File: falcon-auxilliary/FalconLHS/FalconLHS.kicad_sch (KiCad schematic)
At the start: 18 parts, among them J1 100mil, U1 AL8843QSP-13, U2 AL8843QSP-13

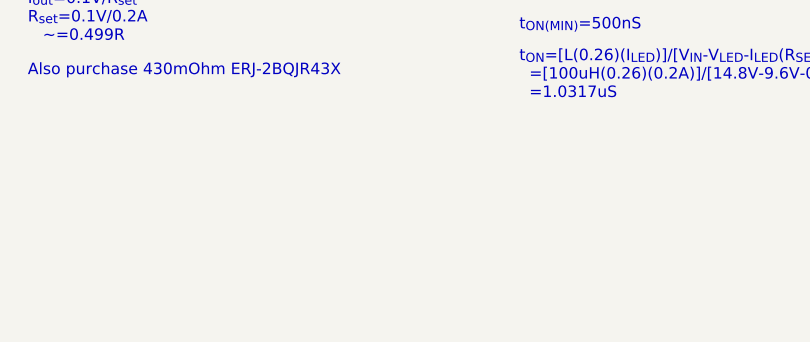
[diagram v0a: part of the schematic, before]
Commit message: Fix missing mounting holes
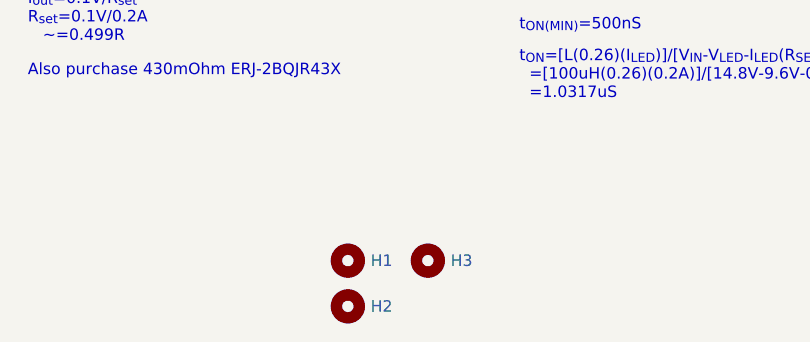
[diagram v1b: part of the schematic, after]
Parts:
- added H1, H2, H3: MountingHole, JetkovKiCADLib:MountingHole_2.7mm_M2.5_Clearanced, symbol Mechanical:MountingHole
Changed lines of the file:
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@@
   (symbol (lib_id "power:GND") (at 187.96 90.17 0) (unit 1)
     (in_bom yes) (on_board yes)
-    (property "Reference" "#PWR07" (id 0) (at 187.96 96.52 0)
+    (property "Reference" "#PWR08" (id 0) (at 187.96 96.52 0)
       (effects (font (size 1.27 1.27)) hide)
     )
@@
   (symbol (lib_id "power:GND") (at 148.59 66.04 0) (mirror y) (unit 1)
     (in_bom yes) (on_board yes)
-    (property "Reference" "#PWR04" (id 0) (at 148.59 72.39 0)
+    (property "Reference" "#PWR05" (id 0) (at 148.59 72.39 0)
       (effects (font (size 1.27 1.27)) hide)
     )
@@
   (symbol (lib_id "power:GND") (at 157.48 66.04 0) (unit 1)
     (in_bom yes) (on_board yes)
-    (property "Reference" "#PWR05" (id 0) (at 157.48 72.39 0)
+    (property "Reference" "#PWR06" (id 0) (at 157.48 72.39 0)
       (effects (font (size 1.27 1.27)) hide)
     )
@@
     (pin "1")
   )
+  (symbol (lib_id "Mechanical:MountingHole") (at 151.13 142.24 0) (unit 1)
+    (in_bom yes) (on_board yes) (fields_autoplaced)
+    (property "Reference" "H3" (id 0) (at 153.67 142.2399 0)
+      (effects (font (size 1.27 1.27)) (justify left))
+    )
+    (property "Value" "MountingHole" (id 1) (at 153.67 143.5099 0)
+      (effects (font (size 1.27 1.27)) (justify left) hide)
+    )
+    (property "Footprint" "JetkovKiCADLib:MountingHole_2.7mm_M2.5_Clearanced" (id 2) (at 151.13 142.24 0)
+      (effects (font (size 1.27 1.27)) hide)
+    )
+    (property "Datasheet" "~" (id 3) (at 151.13 142.24 0)
+      (effects (font (size 1.27 1.27)) hide)
+    )
+  )
   (symbol (lib_id "Device:D_Schottky_Small") (at 96.52 91.44 90) (mirror x) (unit 1)
     (in_bom yes) (on_board yes)
@@
     (pin "2")
   )
+  (symbol (lib_id "Mechanical:MountingHole") (at 142.24 147.32 0) (unit 1)
+    (in_bom yes) (on_board yes) (fields_autoplaced)
+    (property "Reference" "H2" (id 0) (at 144.78 147.3199 0)
+      (effects (font (size 1.27 1.27)) (justify left))
+    )
+    (property "Value" "MountingHole" (id 1) (at 144.78 148.5899 0)
+      (effects (font (size 1.27 1.27)) (justify left) hide)
+    )
+    (property "Footprint" "JetkovKiCADLib:MountingHole_2.7mm_M2.5_Clearanced" (id 2) (at 142.24 147.32 0)
+      (effects (font (size 1.27 1.27)) hide)
+    )
+    (property "Datasheet" "~" (id 3) (at 142.24 147.32 0)
+      (effects (font (size 1.27 1.27)) hide)
+    )
+  )
   (symbol (lib_id "JetkovKiCADLib:XQA LED 1616 SMD") (at 252.73 99.06 0) (mirror x) (unit 1)
     (in_bom yes) (on_board yes)
@@
   (symbol (lib_id "power:GND") (at 64.77 105.41 0) (unit 1)
     (in_bom yes) (on_board yes)
-    (property "Reference" "#PWR?" (id 0) (at 64.77 111.76 0)
+    (property "Reference" "#PWR03" (id 0) (at 64.77 111.76 0)
       (effects (font (size 1.27 1.27)) hide)
     )
@@
   (symbol (lib_id "JetkovKiCADLib:VSYS_SW") (at 187.96 74.93 0) (unit 1)
     (in_bom yes) (on_board yes) (fields_autoplaced)
-    (property "Reference" "#PWR06" (id 0) (at 187.96 78.74 0)
+    (property "Reference" "#PWR07" (id 0) (at 187.96 78.74 0)
       (effects (font (size 1.27 1.27)) hide)
     )
@@
   (symbol (lib_id "power:GND") (at 187.96 105.41 0) (unit 1)
     (in_bom yes) (on_board yes)
-    (property "Reference" "#PWR08" (id 0) (at 187.96 111.76 0)
+    (property "Reference" "#PWR09" (id 0) (at 187.96 111.76 0)
       (effects (font (size 1.27 1.27)) hide)
     )
@@
     (pin "3")
   )
+  (symbol (lib_id "Mechanical:MountingHole") (at 142.24 142.24 0) (unit 1)
+    (in_bom yes) (on_board yes) (fields_autoplaced)
+    (property "Reference" "H1" (id 0) (at 144.78 142.2399 0)
+      (effects (font (size 1.27 1.27)) (justify left))
+    )
+    (property "Value" "MountingHole" (id 1) (at 144.78 143.5099 0)
+      (effects (font (size 1.27 1.27)) (justify left) hide)
+    )
+    (property "Footprint" "JetkovKiCADLib:MountingHole_2.7mm_M2.5_Clearanced" (id 2) (at 142.24 142.24 0)
+      (effects (font (size 1.27 1.27)) hide)
+    )
+    (property "Datasheet" "~" (id 3) (at 142.24 142.24 0)
+      (effects (font (size 1.27 1.27)) hide)
+    )
+  )
   (symbol (lib_id "JetkovKiCADLib:XQA LED 1616 SMD") (at 133.35 90.17 270) (mirror x) (unit 1)
     (in_bom yes) (on_board yes)
@@
   (symbol (lib_id "JetkovKiCADLib:VSYS_SW") (at 148.59 55.88 0) (mirror y) (unit 1)
     (in_bom yes) (on_board yes) (fields_autoplaced)
-    (property "Reference" "#PWR03" (id 0) (at 148.59 59.69 0)
+    (property "Reference" "#PWR04" (id 0) (at 148.59 59.69 0)
       (effects (font (size 1.27 1.27)) hide)
     )
@@
       (reference "#PWR02") (unit 1) (value "GND") (footprint "")
     )
+    (path "/adb484dc-73c8-4e47-871f-1a5ed34a3c70"
+      (reference "#PWR03") (unit 1) (value "GND") (footprint "")
+    )
     (path "/e30e37c4-856b-4345-aee8-f30b69a29ba1"
-      (reference "#PWR03") (unit 1) (value "VSYS_SW") (footprint "")
+      (reference "#PWR04") (unit 1) (value "VSYS_SW") (footprint "")
     )
     (path "/2d99f086-ebd1-4668-abad-9ca91d08ed63"
-      (reference "#PWR04") (unit 1) (value "GND") (footprint "")
+      (reference "#PWR05") (unit 1) (value "GND") (footprint "")
     )
     (path "/50b7ecbc-e4ca-4fa2-aeee-1cb63d2d7299"
-      (reference "#PWR05") (unit 1) (value "GND") (footprint "")
+      (reference "#PWR06") (unit 1) (value "GND") (footprint "")
     )
     (path "/ba40a6a2-1585-45f5-b4d7-9863059f0395"
-      (reference "#PWR06") (unit 1) (value "VSYS_SW") (footprint "")
+      (reference "#PWR07") (unit 1) (value "VSYS_SW") (footprint "")
     )
     (path "/0d1faa69-9753-470f-b5f7-3574ba050c26"
-      (reference "#PWR07") (unit 1) (value "GND") (footprint "")
+      (reference "#PWR08") (unit 1) (value "GND") (footprint "")
     )
     (path "/c399d982-3638-4016-ad00-9edbc6fffd68"
-      (reference "#PWR08") (unit 1) (value "GND") (footprint "")
-    )
-    (path "/adb484dc-73c8-4e47-871f-1a5ed34a3c70"
-      (reference "#PWR?") (unit 1) (value "GND") (footprint "")
+      (reference "#PWR09") (unit 1) (value "GND") (footprint "")
     )
     (path "/1c394162-6cae-4dfe-83f4-2e383531dd08"
@@
       (reference "D8") (unit 1) (value "XQA LED 1616 SMD") (footprint "JetkovKiCADLib:XQ-A-LED_Large")
     )
+    (path "/d26fce45-c1d6-42bc-931d-972bf3799097"
+      (reference "H1") (unit 1) (value "MountingHole") (footprint "JetkovKiCADLib:MountingHole_2.7mm_M2.5_Clearanced")
+    )
+    (path "/99c0b885-9395-4eaa-a204-8d7dea094883"
+      (reference "H2") (unit 1) (value "MountingHole") (footprint "JetkovKiCADLib:MountingHole_2.7mm_M2.5_Clearanced")
+    )
+    (path "/6540157e-dd56-419f-8e12-b9f763e7e5a8"
+      (reference "H3") (unit 1) (value "MountingHole") (footprint "JetkovKiCADLib:MountingHole_2.7mm_M2.5_Clearanced")
+    )
     (path "/d01abbee-7a0e-4e5c-b216-e74fbd323ba1"
